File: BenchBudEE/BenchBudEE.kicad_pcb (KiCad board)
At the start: 4 copper layers, 165.1 x 63.5 mm, 60 parts, among them K1 1461069-5, P1 24Pin MiniFit JR, P2 CONN_3X2, P3 CONN_2, P4 12 Pin Terminal Block, P5 3 Pin TB, Q1 2N3904, Q2 DMN65D8L-7, Q3 MOS_N_NUM, Q4 MOS_N_NUM, U1 LTV-816S, U3 MCP4801, U4 OPA4170, U5 MCP3901, U6 LMT84

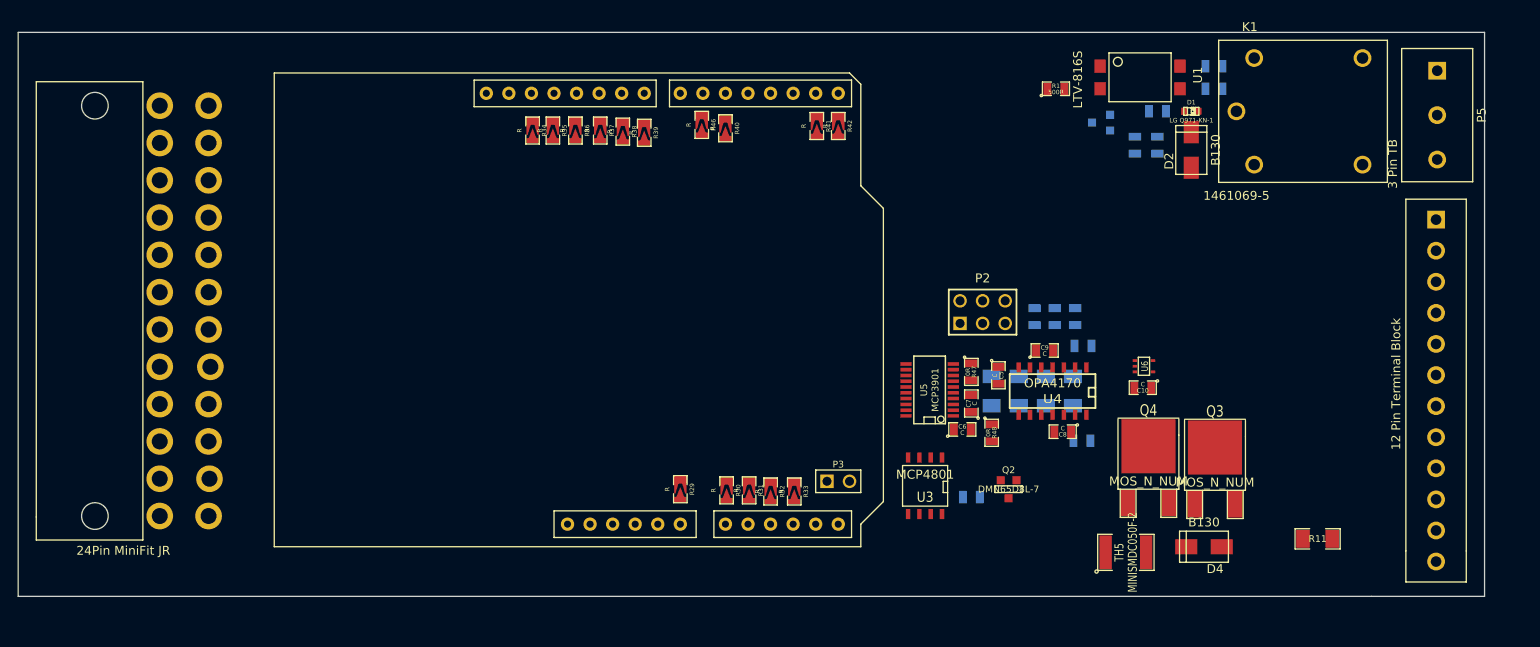
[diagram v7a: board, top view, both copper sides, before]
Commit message: Power Module associated + roughly placed.
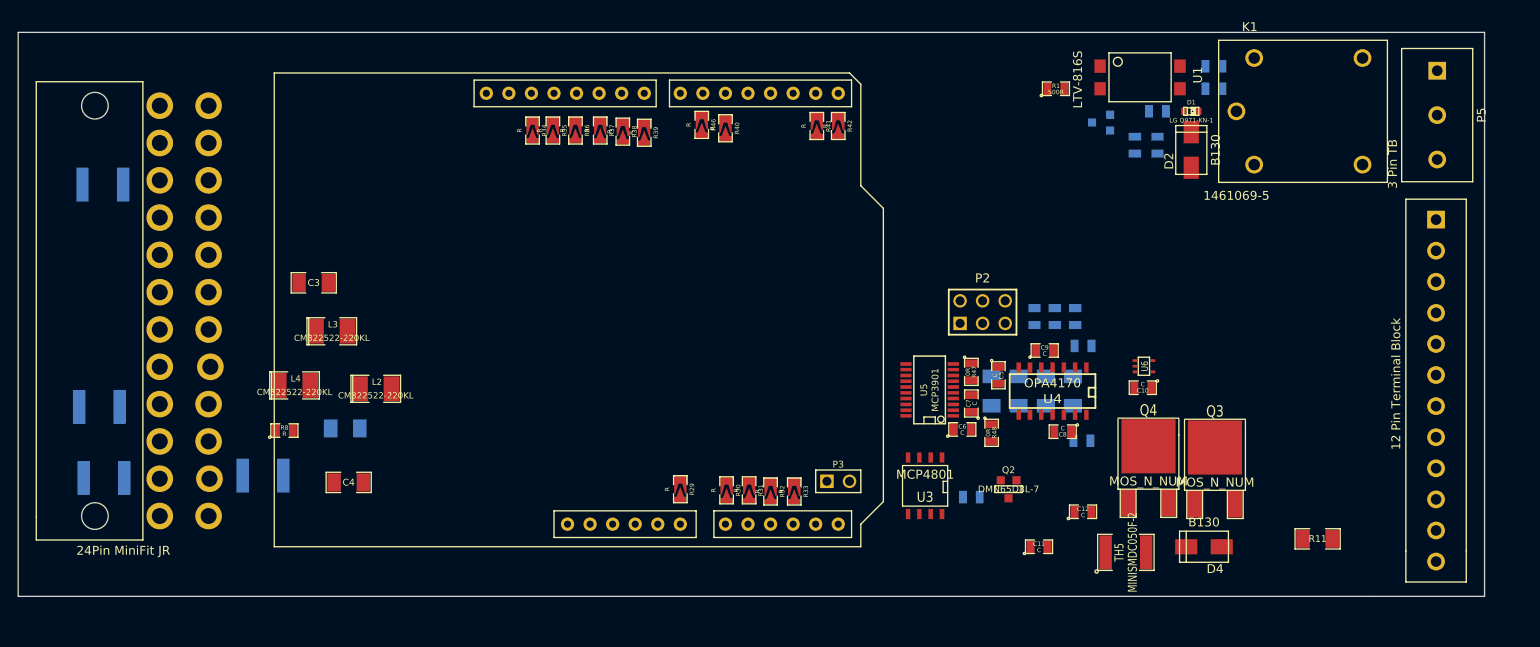
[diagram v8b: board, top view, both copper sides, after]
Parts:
- added C11: C, SM0805, F.Cu at (163.2, 126.5)
- added C12: C, SM0805, F.Cu at (168.1, 122.6)
- added C13: C, SM1206, B.Cu at (85.1, 113.2)
- added C3: C, SM1206, F.Cu at (81.5, 96.8)
- added C4: C, SM1206, F.Cu at (85.5, 119.3)
- added L2: CM322522-220KL, SM1210L, F.Cu at (88.5, 108.7)
- added L3: CM322522-220KL, SM1210L, F.Cu at (83.6, 102.2)
- added L4: CM322522-220KL, SM1210L, F.Cu at (79.4, 108.3)
- added R8: R, SM0805, F.Cu at (78.2, 113.4)
- added TH1: MINISMDC050F-2, SM1812, B.Cu at (57.9, 118.7)
- added TH2: MINISMDC050F-2, SM1812, B.Cu at (57.4, 110.7)
- added TH3: MINISMDC050F-2, SM1812, B.Cu at (57.8, 85.7)
- added TH4: MINISMDC050F-2, SM1812, B.Cu at (75.8, 118.5)
